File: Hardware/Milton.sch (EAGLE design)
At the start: 75 parts, among them J1 1981568-1, Q1 12MHz, U10 MAX31850K, U3 USD-SOCKETNEW, U4 MMA8452Q, U5 MIC5203-5.0YM5, U6 SI4464, U7 TPS61201, U8 BME280, U9 MMDT3904, X1 B4B-ZR

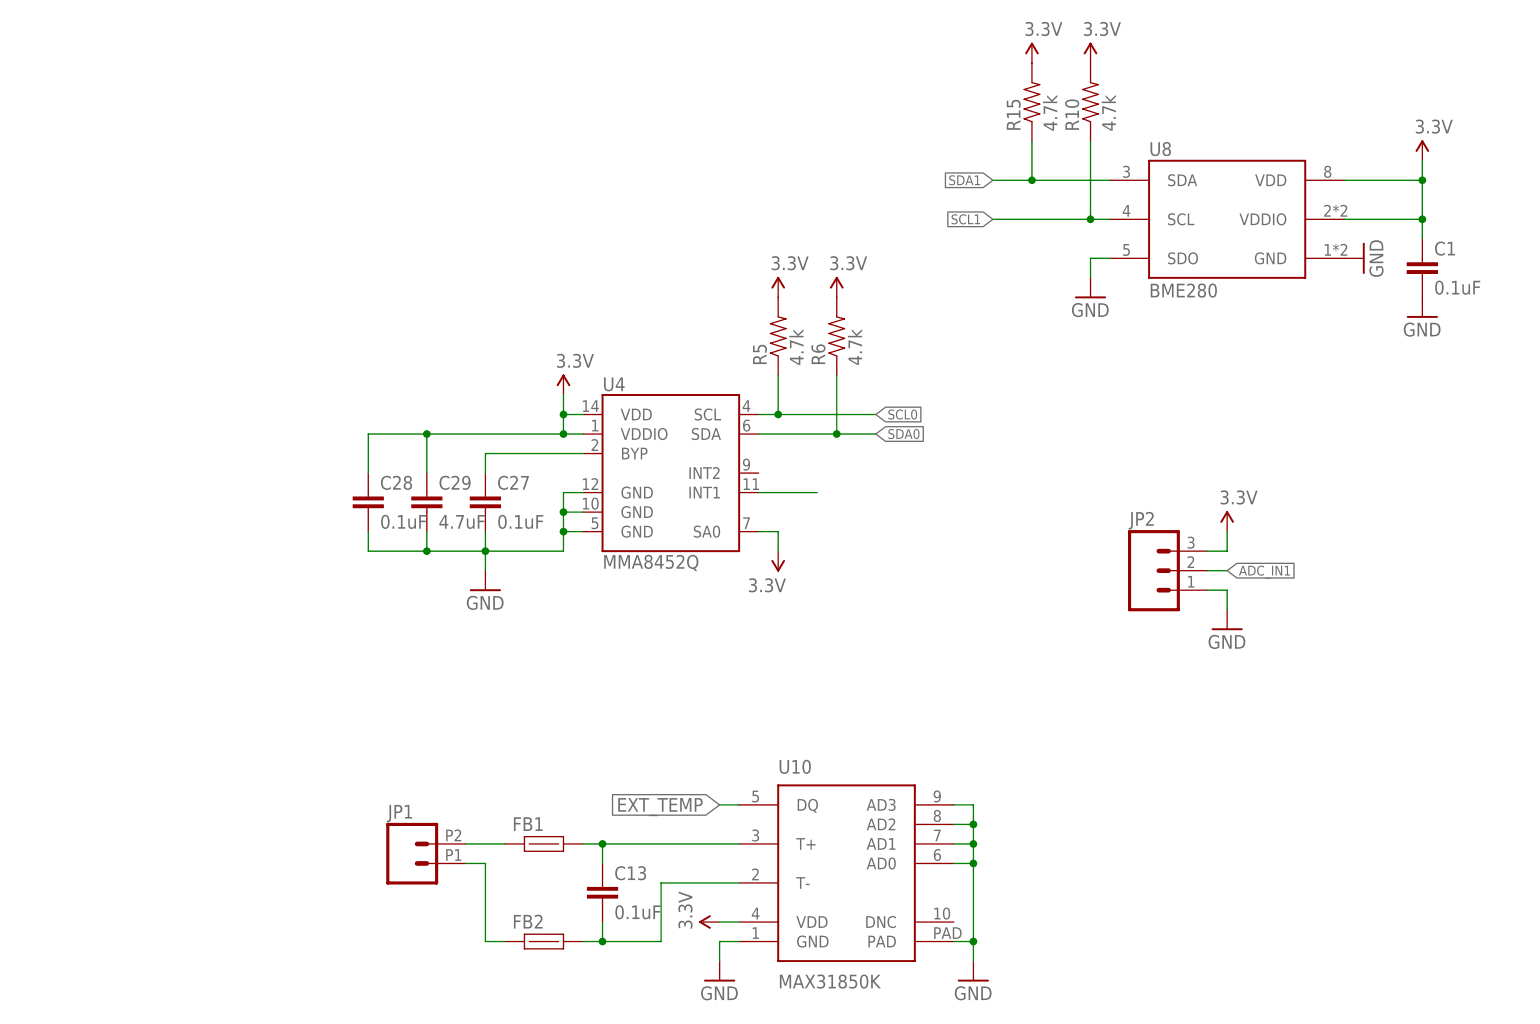
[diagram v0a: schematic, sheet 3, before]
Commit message: Cleaning
Optimize traces, add more part numbers.
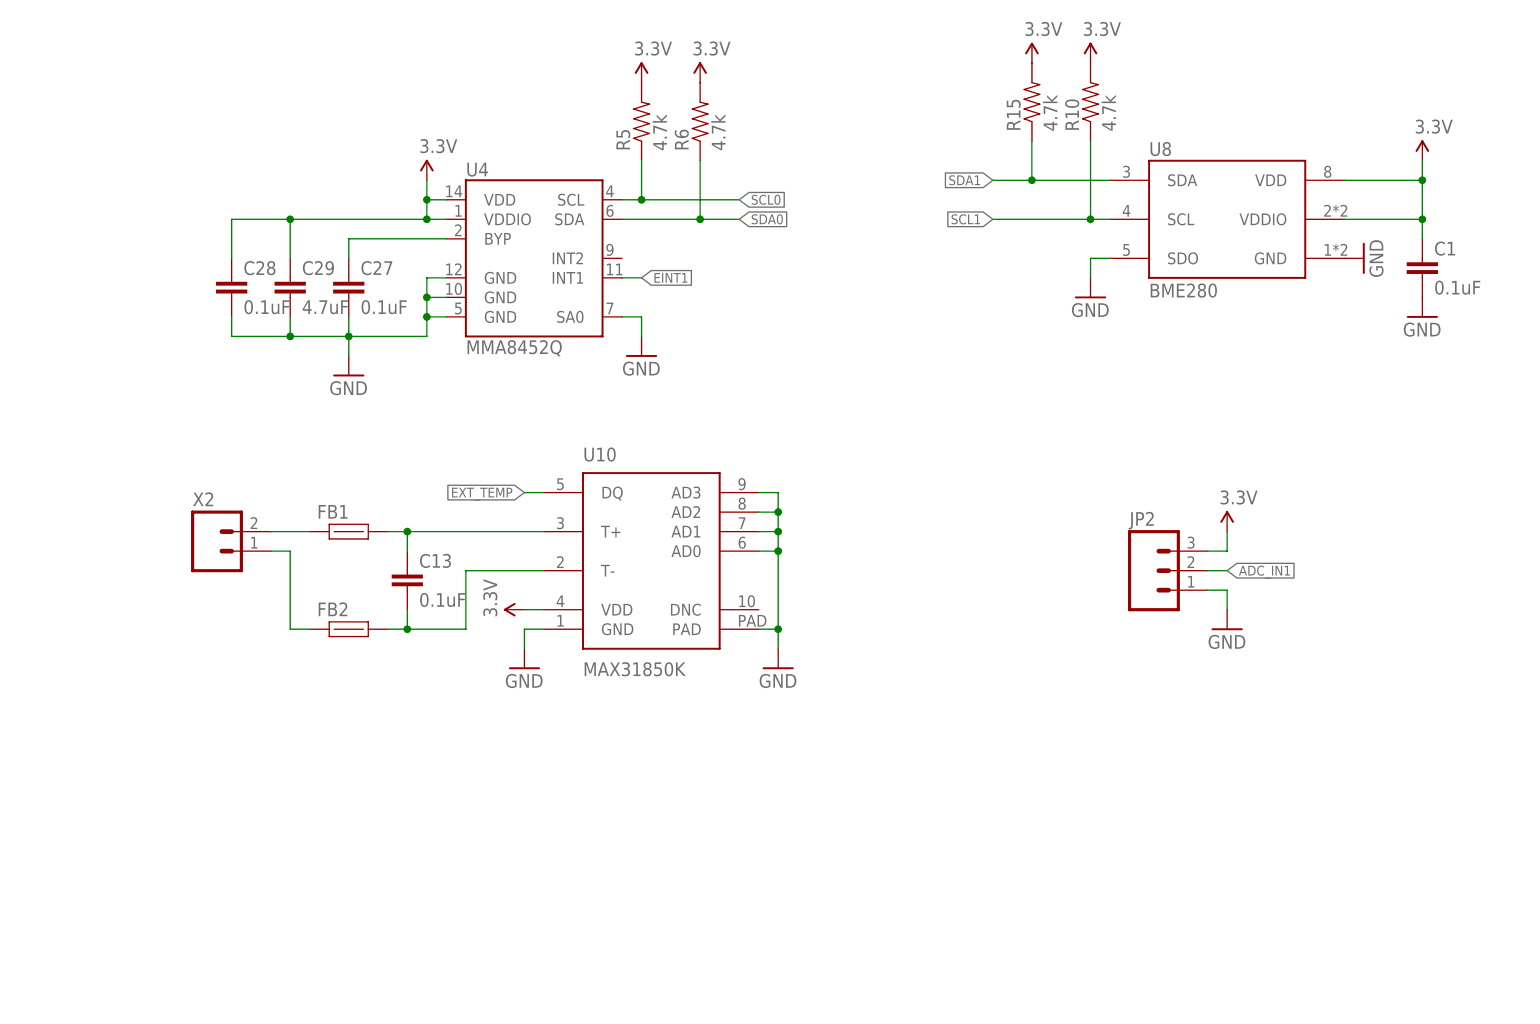
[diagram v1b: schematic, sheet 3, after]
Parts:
- removed C21: 0.47uF, SparkFun-Capacitors:CAP0603-CAP
- removed JP1: M022.54MM_SCREWTERM, SparkFun-Connectors:M022.54MM_SCREWTERM
- removed U9: MMDT3904, SparkFun-DiscreteSemi:MMDT3904
- added C22, C32: 0.1uF, SparkFun-Capacitors:CAP0603-CAP
- added R11: 180k, SparkFun-Resistors:RESISTOR0603
- added R3: 4.7k, SparkFun-Resistors:RESISTOR0603
- added R7: 10k, SparkFun-Resistors:RESISTOR0603
- added R9: 1M, SparkFun-Resistors:RESISTOR0603
- added U2: DDC113TU-7-F, wrea:DDC113TU-7-F
- added X2: M023.5MM, SparkFun-Connectors:M023.5MM
- C1, C10, C11, C13, C19, C27, C28, C3, C8, C9: PARTNO CL10B104KO8NNNC -> (none)
- C25, C26: MPN (none) -> CL10C470JB8NCNC
- C29: MPN (none) -> CC0603KRX5R6BB475
- C7: value 100nf -> 0.1uF; MPN (none) -> CL10B104KO8NNNC
- JP5: MPN (none) -> S2B-PH-K-S(LF)(SN)
- Q1: PARTNO 7V-12.000MAHE-T -> (none)
- R1, R2: MPN (none) -> MCR03ERTJ270
- R8: MPN RMCF0603JT10K0 -> ESR03EZPJ103; PARTNO RMCF0603JT10K0 -> (none)
- U10: MPN (none) -> MAX31850TATB+
- U5: value MIC5203-5.0YM5 -> TCR2EE50,LM; device wrea:MIC5203-5.0YM5 -> Xevelabs:IC_TCR2EEESV; MPN MIC5203-5.0YM5 TR -> (none)
- U6: MPN (none) -> SI4464-B1B-FM
- U7: value TPS61201 -> TPS61200; device texas:TPS61201 -> texas:TPS61200
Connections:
- removed net N$16: U4.INT1
- new net N$1: R11.2, R9.1, U7.FB
- new net N$10: J1.5, R3.2
- new net N$21: R3.1, R7.2, U$3.CBUS0
- net 3.3V: now also C32.1, R9.2, U5.VIN; no longer U4.SA0, U5.IN, U7.FB
- net 5V: now also C22.1, U2G$1.C, U2G$2.C, U5.VOUT; no longer C21.2, U5.OUT, U9G$1.C, U9G$2.C
- net CAM1: now also U2G$1.E; no longer U9G$1.E
- net CAM2: now also U2G$2.E; no longer U9G$2.E
- net CAMERA1_EN: now also U2G$1.B; no longer U9G$1.B
- net CAMERA2_EN: now also U2G$2.B; no longer U9G$2.B
- net EINT1: now also U4.INT1
- net GND: now also C22.2, C32.2, R11.1, R7.1, U4.SA0; no longer C21.1
- net TM_RAW: now also X2.1; no longer JP1.1
- net TP_RAW: now also X2.2; no longer JP1.2
- net VIN: no longer J1.5, U$3.CBUS0
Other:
- moved on the sheet: C13, C19, C20, C26, C27, C28, C29, FB1, FB2, R5, R6, U10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

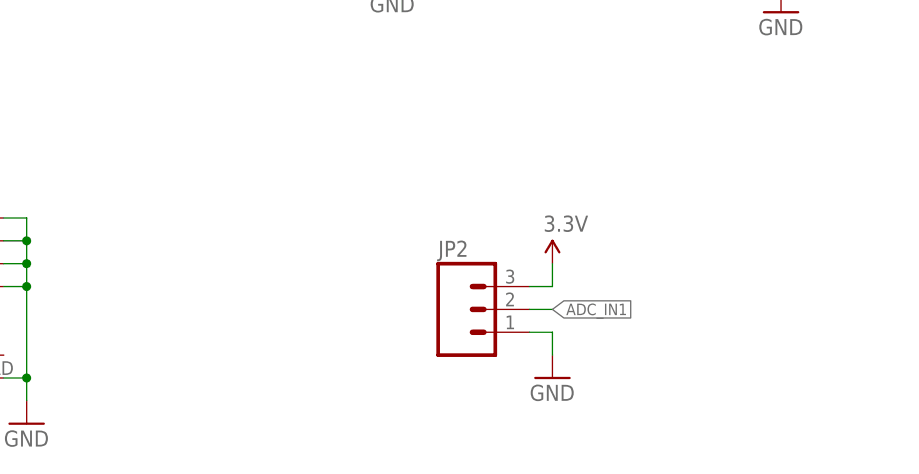
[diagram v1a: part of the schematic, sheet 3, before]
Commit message: Update.
Shifted components to make room to break out another digital io
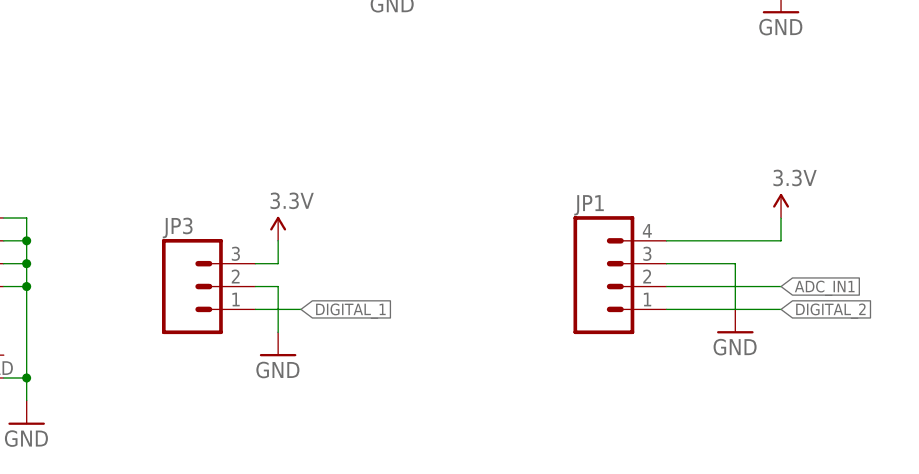
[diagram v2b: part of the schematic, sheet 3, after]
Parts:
- removed J1: 1981568-1, wrea:1981568-1
- removed JP2: (no value), SparkFun-Connectors:M03LOCK
- added JP1: (no value), SparkFun-Connectors:M04PTH
- added U$5: USB-CON-5PIN-105017-0001, GeekAmmo:USB-CON-5PIN-105017-0001
- U7: MPN (none) -> TPS61200DRCR
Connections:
- removed net CUTDOWN: JP3.2, U1.P2[2]/PWM1[3]/CTS1/TRACEDATA[3]
- new net DIGITAL_1: JP3.1, U1.P2[2]/PWM1[3]/CTS1/TRACEDATA[3]
- new net DIGITAL_2: JP1.1, U1.P0[25]/AD0[2]/I2SRX_SDA/TXD3
- net 3.3V: now also JP1.4; no longer JP2.3
- net ADC_IN1: now also JP1.2; no longer JP2.2
- net GND: now also JP1.3, JP3.2, U$5.GND; no longer J1.1, JP2.1, JP3.1
- net N$10: now also U$5.VBUS; no longer J1.5
- net N$7: now also U$5.D+; no longer J1.3
- net N$9: now also U$5.D-; no longer J1.4
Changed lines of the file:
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@@
 <layer number="60" name="p_dimension" color="6" fill="0" visible="no" active="no"/>
 <layer number="61" name="pt_docu" color="7" fill="0" visible="no" active="no"/>
+<layer number="90" name="Modules" color="5" fill="1" visible="yes" active="yes"/>
 <layer number="91" name="Nets" color="2" fill="1" visible="yes" active="yes"/>
 <layer number="92" name="Busses" color="1" fill="1" visible="yes" active="yes"/>
@@
 <attribute name="MPN" value="C0603C180K3GACTU"/>
 </part>
-<part name="U7" library="texas" deviceset="TPS6120*" device="" technology="0" value="TPS61200"/>
+<part name="U7" library="texas" deviceset="TPS6120*" device="" technology="0" value="TPS61200">
+<attribute name="MPN" value="TPS61200DRCR"/>
+</part>
 <part name="GND28" library="SparkFun-Aesthetics" deviceset="GND" device=""/>
 <part name="GND29" library="SparkFun-Aesthetics" deviceset="GND" device=""/>
@@
 <part name="SUPPLY2" library="SparkFun-Aesthetics" deviceset="3.3V" device=""/>
 <part name="GND4" library="supply1" deviceset="GND" device=""/>
-<part name="J1" library="wrea" deviceset="1981568-1" device=""/>
 <part name="GND15" library="supply1" deviceset="GND" device=""/>
 <part name="R1" library="SparkFun-Resistors" deviceset="RESISTOR" device="0603" value="27">
@@
 <part name="GND11" library="SparkFun" deviceset="GND" device=""/>
 <part name="GND26" library="SparkFun" deviceset="GND" device=""/>
-<part name="JP2" library="SparkFun-Connectors" deviceset="M03" device="LOCK"/>
 <part name="P+6" library="SparkFun" deviceset="3.3V" device=""/>
 <part name="GND1" library="SparkFun" deviceset="GND" device=""/>
@@
 </part>
 <part name="GND25" library="SparkFun" deviceset="GND" device=""/>
+<part name="U$5" library="GeekAmmo" deviceset="USB-CON-5PIN" device="-105017-0001"/>
+<part name="JP1" library="SparkFun-Connectors" deviceset="M04" device="PTH"/>
 </parts>
 <sheets>
@@
 <instance part="SUPPLY2" gate="G$1" x="-20.32" y="111.76"/>
 <instance part="GND4" gate="1" x="-43.18" y="68.58"/>
-<instance part="J1" gate="A" x="-83.82" y="81.28" rot="R180"/>
 <instance part="GND15" gate="1" x="-81.28" y="76.2"/>
 <instance part="R1" gate="G$1" x="-68.58" y="86.36">
@@
 <instance part="X1" gate="-4" x="284.48" y="7.62" rot="R270"/>
 <instance part="SUPPLY9" gate="G$1" x="297.18" y="35.56" rot="R270"/>
-<instance part="JP3" gate="G$1" x="-68.58" y="160.02"/>
-<instance part="SUPPLY10" gate="G$1" x="-58.42" y="165.1"/>
-<instance part="GND27" gate="1" x="-58.42" y="152.4"/>
 <instance part="ISP" gate="G$1" x="200.66" y="15.24" rot="R90"/>
 <instance part="GND30" gate="1" x="200.66" y="7.62"/>
@@
 <attribute name="MPN" x="279.4" y="22.86" size="1.27" layer="96" display="off"/>
 </instance>
+<instance part="U$5" gate="G$1" x="-93.98" y="86.36"/>
 </instances>
 <busses>
@@
 </segment>
 <segment>
-<pinref part="J1" gate="A" pin="1"/>
 <pinref part="GND15" gate="1" pin="GND"/>
 <wire x1="-83.82" y1="81.28" x2="-81.28" y2="81.28" width="0.1524" layer="91"/>
 <wire x1="-81.28" y1="81.28" x2="-81.28" y2="78.74" width="0.1524" layer="91"/>
+<pinref part="U$5" gate="G$1" pin="GND"/>
 </segment>
 <segment>
@@
 <wire x1="289.56" y1="15.24" x2="287.02" y2="15.24" width="0.1524" layer="91"/>
 <junction x="287.02" y="15.24"/>
-</segment>
-<segment>
-<pinref part="JP3" gate="G$1" pin="1"/>
-<pinref part="GND27" gate="1" pin="GND"/>
-<wire x1="-60.96" y1="157.48" x2="-58.42" y2="157.48" width="0.1524" layer="91"/>
-<wire x1="-58.42" y1="157.48" x2="-58.42" y2="154.94" width="0.1524" layer="91"/>
 </segment>
 <segment>
@@
 <pinref part="P+1" gate="G$1" pin="3.3V"/>
 </segment>
-<segment>
-<pinref part="JP3" gate="G$1" pin="3"/>
-<pinref part="SUPPLY10" gate="G$1" pin="3.3V"/>
-<wire x1="-60.96" y1="162.56" x2="-58.42" y2="162.56" width="0.1524" layer="91"/>
-<wire x1="-58.42" y1="162.56" x2="-58.42" y2="165.1" width="0.1524" layer="91"/>
-</segment>
 </net>
 <net name="TXD1" class="0">
@@
 </segment>
 </net>
-<net name="CUTDOWN" class="0">
-<segment>
-<pinref part="JP3" gate="G$1" pin="2"/>
-<wire x1="-55.88" y1="160.02" x2="-60.96" y2="160.02" width="0.1524" layer="91"/>
-<label x="-55.88" y="160.02" size="1.27" layer="95" xref="yes"/>
-</segment>
+<net name="DIGITAL_1" class="0">
 <segment>
 <pinref part="U1" gate="G$1" pin="P2[2]/PWM1[3]/CTS1/TRACEDATA[3]"/>
@@
 <segment>
 <pinref part="R1" gate="G$1" pin="1"/>
-<pinref part="J1" gate="A" pin="3"/>
 <wire x1="-83.82" y1="86.36" x2="-73.66" y2="86.36" width="0.1524" layer="91"/>
+<pinref part="U$5" gate="G$1" pin="D+"/>
 </segment>
 </net>
@@
 <segment>
 <pinref part="R2" gate="G$1" pin="1"/>
-<pinref part="J1" gate="A" pin="4"/>
 <wire x1="-83.82" y1="88.9" x2="-60.96" y2="88.9" width="0.1524" layer="91"/>
 <pinref part="C26" gate="G$1" pin="2"/>
@@
 <wire x1="-60.96" y1="88.9" x2="-60.96" y2="91.44" width="0.1524" layer="91"/>
 <junction x="-60.96" y="88.9"/>
+<pinref part="U$5" gate="G$1" pin="D-"/>
 </segment>
 </net>
@@
 <net name="N$10" class="0">
 <segment>
-<pinref part="J1" gate="A" pin="5"/>
 <wire x1="-83.82" y1="91.44" x2="-76.2" y2="91.44" width="0.1524" layer="91"/>
 <pinref part="R3" gate="G$1" pin="2"/>
 <wire x1="-76.2" y1="91.44" x2="-76.2" y2="68.58" width="0.1524" layer="91"/>
+<pinref part="U$5" gate="G$1" pin="VBUS"/>
 </segment>
 </net>
@@
 <wire x1="-68.58" y1="27.94" x2="12.7" y2="27.94" width="0.1524" layer="91"/>
 <wire x1="12.7" y1="27.94" x2="12.7" y2="30.48" width="0.1524" layer="91"/>
+</segment>
+</net>
+<net name="DIGITAL_2" class="0">
+<segment>
+<pinref part="U1" gate="G$1" pin="P0[25]/AD0[2]/I2SRX_SDA/TXD3"/>
+<wire x1="55.88" y1="119.38" x2="60.96" y2="119.38" width="0.1524" layer="91"/>
+<label x="55.88" y="119.38" size="1.27" layer="95" rot="R180" xref="yes"/>
 </segment>
 </net>
@@
 <instance part="GND11" gate="1" x="53.34" y="50.8"/>
 <instance part="GND26" gate="1" x="86.36" y="50.8"/>
-<instance part="JP2" gate="G$1" x="134.62" y="63.5"/>
-<instance part="P+6" gate="G$1" x="144.78" y="68.58"/>
-<instance part="GND1" gate="1" x="144.78" y="55.88"/>
+<instance part="P+6" gate="G$1" x="170.18" y="73.66"/>
+<instance part="GND1" gate="1" x="165.1" y="60.96"/>
 <instance part="GND25" gate="1" x="68.58" y="91.44"/>
+<instance part="JP1" gate="G$1" x="152.4" y="66.04"/>
+<instance part="JP3" gate="G$1" x="104.14" y="66.04"/>
+<instance part="SUPPLY10" gate="G$1" x="114.3" y="71.12"/>
+<instance part="GND27" gate="1" x="114.3" y="58.42"/>
 </instances>
 <busses>
@@
 </segment>
 <segment>
-<pinref part="JP2" gate="G$1" pin="1"/>
-<pinref part="GND1" gate="1" pin="GND"/>
-<wire x1="142.24" y1="60.96" x2="144.78" y2="60.96" width="0.1524" layer="91"/>
-<wire x1="144.78" y1="60.96" x2="144.78" y2="58.42" width="0.1524" layer="91"/>
-</segment>
-<segment>
 <pinref part="U4" gate="G$1" pin="SA0"/>
 <wire x1="66.04" y1="96.52" x2="68.58" y2="96.52" width="0.1524" layer="91"/>
 <wire x1="68.58" y1="96.52" x2="68.58" y2="93.98" width="0.1524" layer="91"/>
 <pinref part="GND25" gate="1" pin="GND"/>
+</segment>
+<segment>
+<pinref part="GND1" gate="1" pin="GND"/>
+<wire x1="157.48" y1="68.58" x2="165.1" y2="68.58" width="0.1524" layer="91"/>
+<wire x1="165.1" y1="68.58" x2="165.1" y2="63.5" width="0.1524" layer="91"/>
+<pinref part="JP1" gate="G$1" pin="3"/>
+</segment>
+<segment>
+<pinref part="JP3" gate="G$1" pin="2"/>
+<pinref part="GND27" gate="1" pin="GND"/>
+<wire x1="111.76" y1="66.04" x2="114.3" y2="66.04" width="0.1524" layer="91"/>
+<wire x1="114.3" y1="66.04" x2="114.3" y2="60.96" width="0.1524" layer="91"/>
 </segment>
 </net>
@@
 </segment>
 <segment>
-<pinref part="JP2" gate="G$1" pin="3"/>
 <pinref part="P+6" gate="G$1" pin="3.3V"/>
-<wire x1="142.24" y1="66.04" x2="144.78" y2="66.04" width="0.1524" layer="91"/>
-<wire x1="144.78" y1="66.04" x2="144.78" y2="68.58" width="0.1524" layer="91"/>
+<wire x1="157.48" y1="71.12" x2="170.18" y2="71.12" width="0.1524" layer="91"/>
+<wire x1="170.18" y1="71.12" x2="170.18" y2="73.66" width="0.1524" layer="91"/>
+<pinref part="JP1" gate="G$1" pin="4"/>
+</segment>
+<segment>
+<pinref part="JP3" gate="G$1" pin="3"/>
+<pinref part="SUPPLY10" gate="G$1" pin="3.3V"/>
+<wire x1="111.76" y1="68.58" x2="114.3" y2="68.58" width="0.1524" layer="91"/>
+<wire x1="114.3" y1="68.58" x2="114.3" y2="71.12" width="0.1524" layer="91"/>
 </segment>
 </net>
@@
 <net name="ADC_IN1" class="0">
 <segment>
-<pinref part="JP2" gate="G$1" pin="2"/>
-<wire x1="144.78" y1="63.5" x2="142.24" y2="63.5" width="0.1524" layer="91"/>
-<label x="144.78" y="63.5" size="1.27" layer="95" xref="yes"/>
-</segment>
-</net>
+<wire x1="170.18" y1="66.04" x2="157.48" y2="66.04" width="0.1524" layer="91"/>
+<label x="170.18" y="66.04" size="1.27" layer="95" xref="yes"/>
+<pinref part="JP1" gate="G$1" pin="2"/>
+</segment>
+</net>
+<net name="DIGITAL_2" class="0">
+<segment>
+<pinref part="JP1" gate="G$1" pin="1"/>
+<wire x1="170.18" y1="63.5" x2="157.48" y2="63.5" width="0.1524" layer="91"/>
+<label x="170.18" y="63.5" size="1.27" layer="95" xref="yes"/>
+</segment>
+</net>
+<net name="DIGITAL_1" class="0">
+<segment>
+<wire x1="116.84" y1="63.5" x2="111.76" y2="63.5" width="0.1524" layer="91"/>
+<label x="116.84" y="63.5" size="1.27" layer="95" xref="yes"/>
+<pinref part="JP3" gate="G$1" pin="1"/>
+</segment>
+</net>
